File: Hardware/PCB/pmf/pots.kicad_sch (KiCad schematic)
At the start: 39 parts, among them U3 TL074, U4 TL072

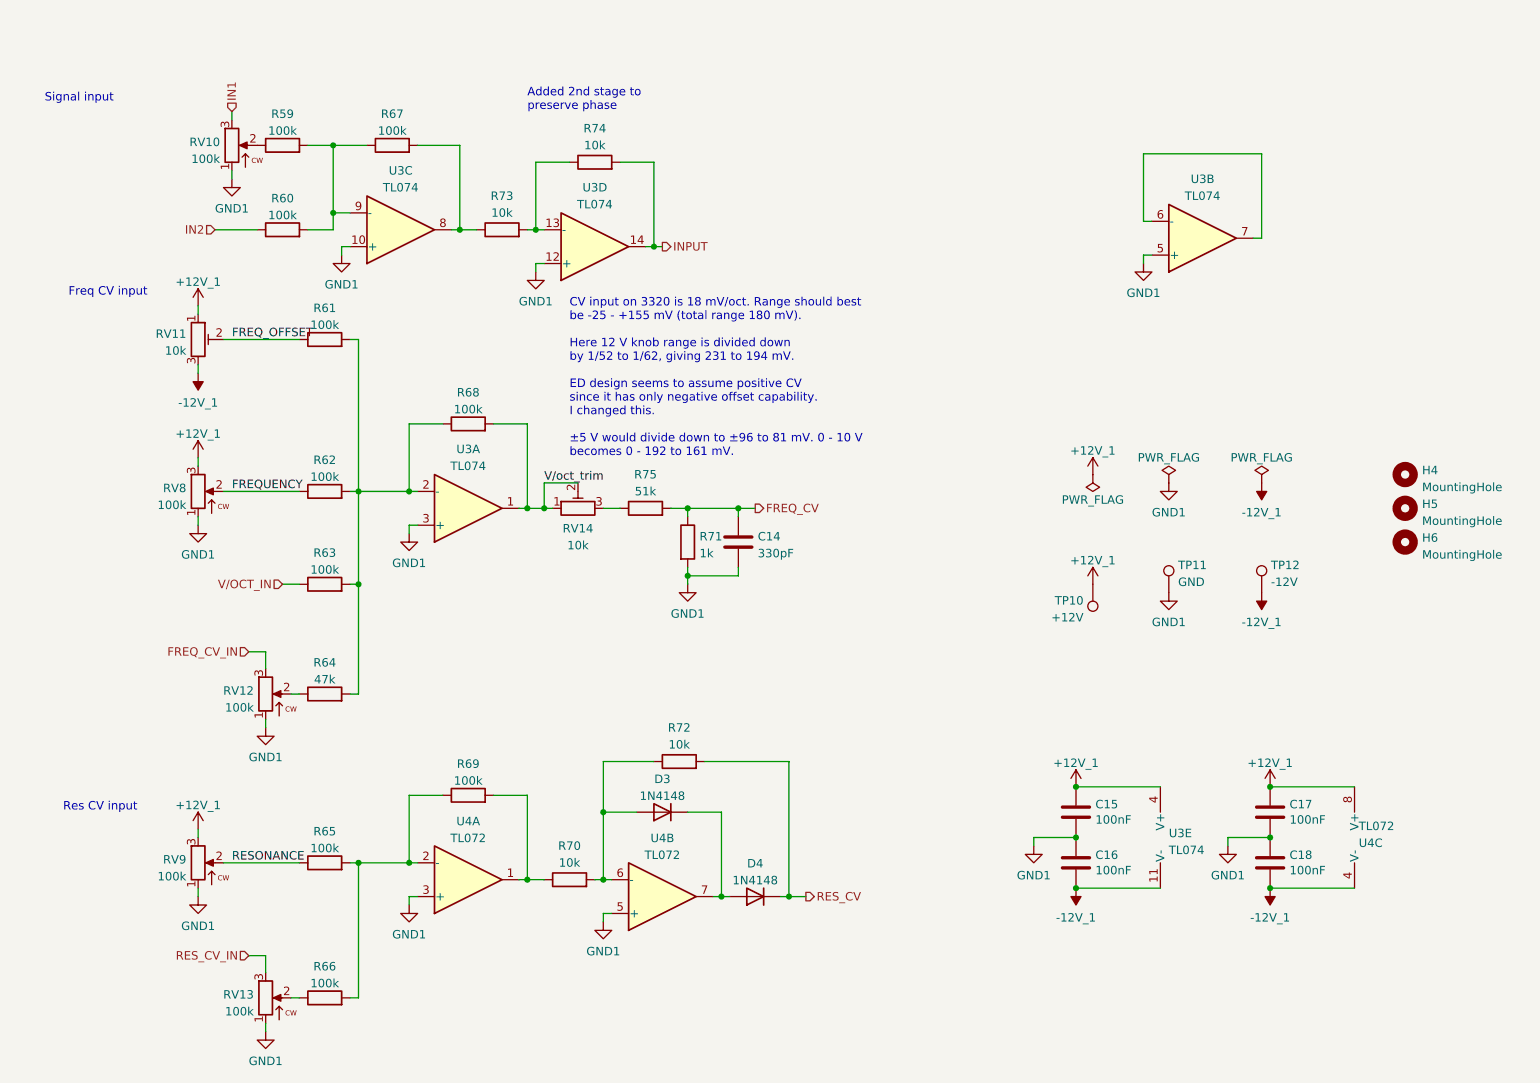
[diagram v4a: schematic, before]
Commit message: Remove VRES bias
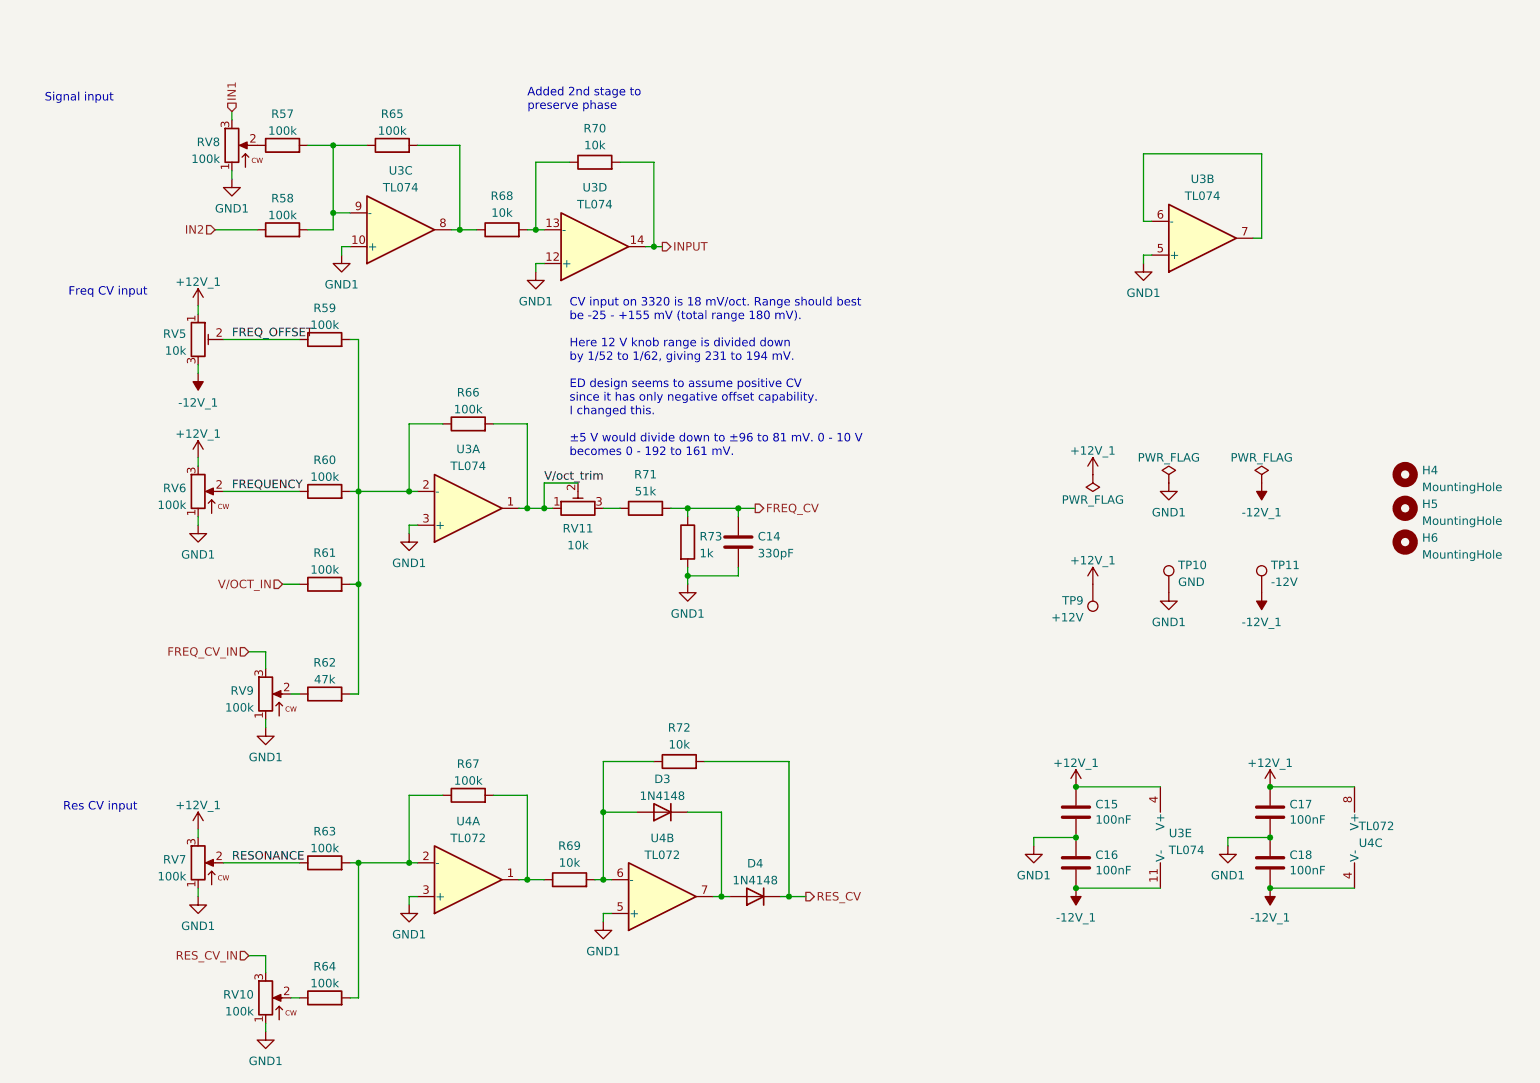
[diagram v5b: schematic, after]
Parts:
- renumbered R59 to R57, R60 to R58, R61 to R59, R62 to R60, R63 to R61, R64 to R62, R65 to R63, R66 to R64, R67 to R65, R68 to R66, R69 to R67, R73 to R68, R70 to R69, R74 to R70, R75 to R71, R71 to R73, RV13 to RV10, RV14 to RV11, RV11 to RV5, RV8 to RV6, RV9 to RV7, RV10 to RV8, RV12 to RV9, TP11 to TP10, TP12 to TP11, TP10 to TP9

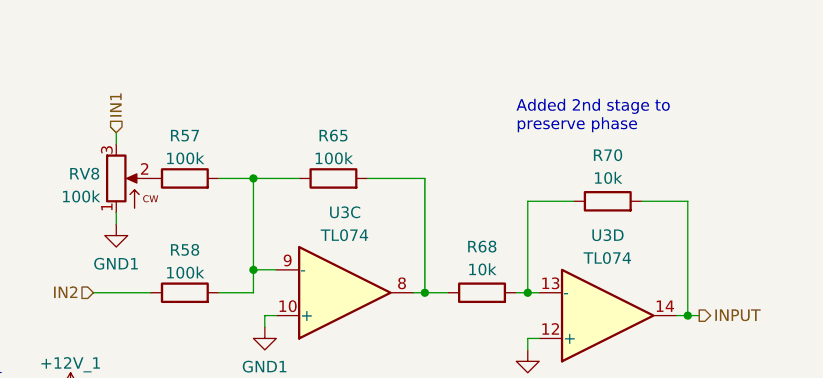
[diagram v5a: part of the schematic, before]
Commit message: Reduce amplitude at input and restore at output
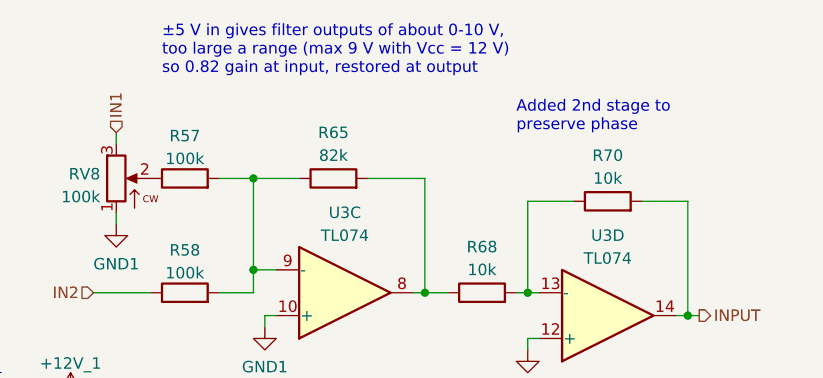
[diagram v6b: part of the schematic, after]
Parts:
- R65: value 100k -> 82k
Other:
- note added: "±5 V in gives filter outputs of about 0-10 V, too large a range (max 9 V with Vcc = 12 V) so 0.82 gain at input, restored at output"
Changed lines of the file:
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@@
+    (effects (font (size 1.27 1.27)) (justify left bottom))
+  )
+  (text "±5 V in gives filter outputs of about 0-10 V,\ntoo large a range (max 9 V with Vcc = 12 V)\nso 0.82 gain at input, restored at output"
+    (at 73.66 24.13 0)
     (effects (font (size 1.27 1.27)) (justify left bottom))
   )
@@
   (symbol (lib_id "AO_symbols:R") (at 92.71 35.56 90) (unit 1)
     (in_bom yes) (on_board yes) (dnp no) (fields_autoplaced)
-    (property "Reference" "R65" (at 92.71 30.8442 90)
-      (effects (font (size 1.27 1.27)))
-    )
-    (property "Value" "100k" (at 92.71 33.3811 90)
-      (effects (font (size 1.27 1.27)))
-    )
+    (property "Reference" "R65" (at 92.71 30.48 90)
+      (effects (font (size 1.27 1.27)))
+    )
+    (property "Value" "82k" (at 92.71 33.02 90)
+      (effects (font (size 1.27 1.27)))
+    )

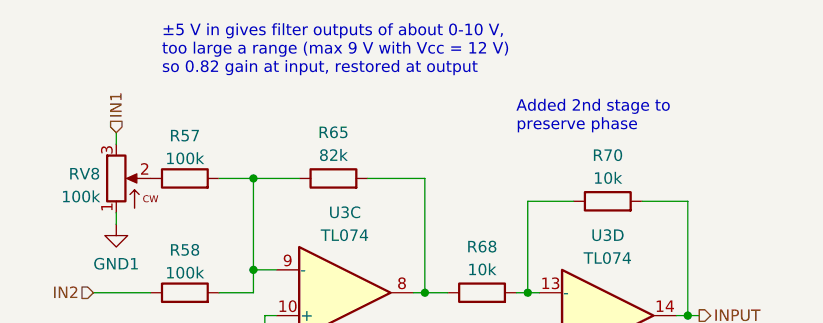
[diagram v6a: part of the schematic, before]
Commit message: Lower gain at input and higher at output; better justification for AC coupling at compensation mixer
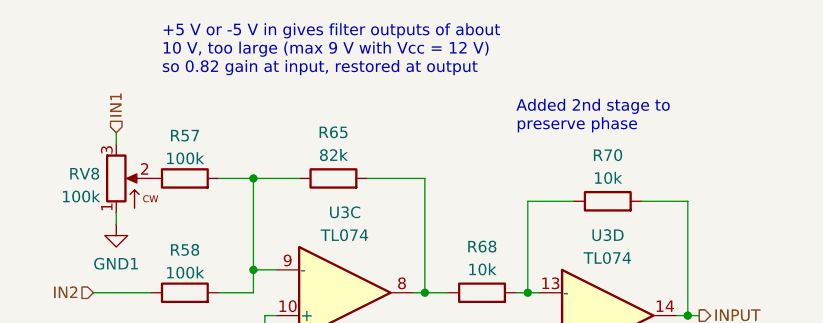
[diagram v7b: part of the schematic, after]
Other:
- note added: "+5 V or -5 V in gives filter outputs of about 10 V, too large (max 9 V with Vcc = 12 V) so 0.82 gain at input, restored at output"
- note removed: "±5 V in gives filter outputs of about 0-10 V, too large a range (max 9 V with Vcc = 12 V) so 0.82 gain at input, restored at output"
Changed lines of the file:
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@@
     (effects (font (size 1.27 1.27)) (justify left bottom))
   )
-  (text "±5 V in gives filter outputs of about 0-10 V,\ntoo large a range (max 9 V with Vcc = 12 V)\nso 0.82 gain at input, restored at output"
+  (text "+5 V or -5 V in gives filter outputs of about \n10 V, too large (max 9 V with Vcc = 12 V)\nso 0.82 gain at input, restored at output"
     (at 73.66 24.13 0)
     (effects (font (size 1.27 1.27)) (justify left bottom))

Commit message: Large attenuation and amplification
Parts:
- R65: value 82k -> 51k
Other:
- note added: "+5 V or -5 V in gives filter outputs of about 10 V without resonance and even more with, too large (max 9 V with Vcc = 12 V) so 0.51 gain at input, restored at output"
- note removed: "+5 V or -5 V in gives filter outputs of about 10 V, too large (max 9 V with Vcc = 12 V) so 0.82 gain at input, restored at output"
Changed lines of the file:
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@@
     (effects (font (size 1.27 1.27)) (justify left bottom))
   )
-  (text "+5 V or -5 V in gives filter outputs of about \n10 V, too large (max 9 V with Vcc = 12 V)\nso 0.82 gain at input, restored at output"
+  (text "+5 V or -5 V in gives filter outputs of about \n10 V without resonance and even more with, \ntoo large (max 9 V with Vcc = 12 V)\nso 0.51 gain at input, restored at output"
     (at 73.66 24.13 0)
     (effects (font (size 1.27 1.27)) (justify left bottom))
@@
       (effects (font (size 1.27 1.27)))
     )
-    (property "Value" "82k" (at 92.71 33.02 90)
-      (effects (font (size 1.27 1.27)))
-    )
+    (property "Value" "51k" (at 92.71 33.02 90)
+      (effects (font (size 1.27 1.27)))
+    )
